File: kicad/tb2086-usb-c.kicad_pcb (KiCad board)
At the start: 2 copper layers, 29.3 x 19.5 mm, 17 parts, among them J1 Conn_01x04, U1 SRV05-4

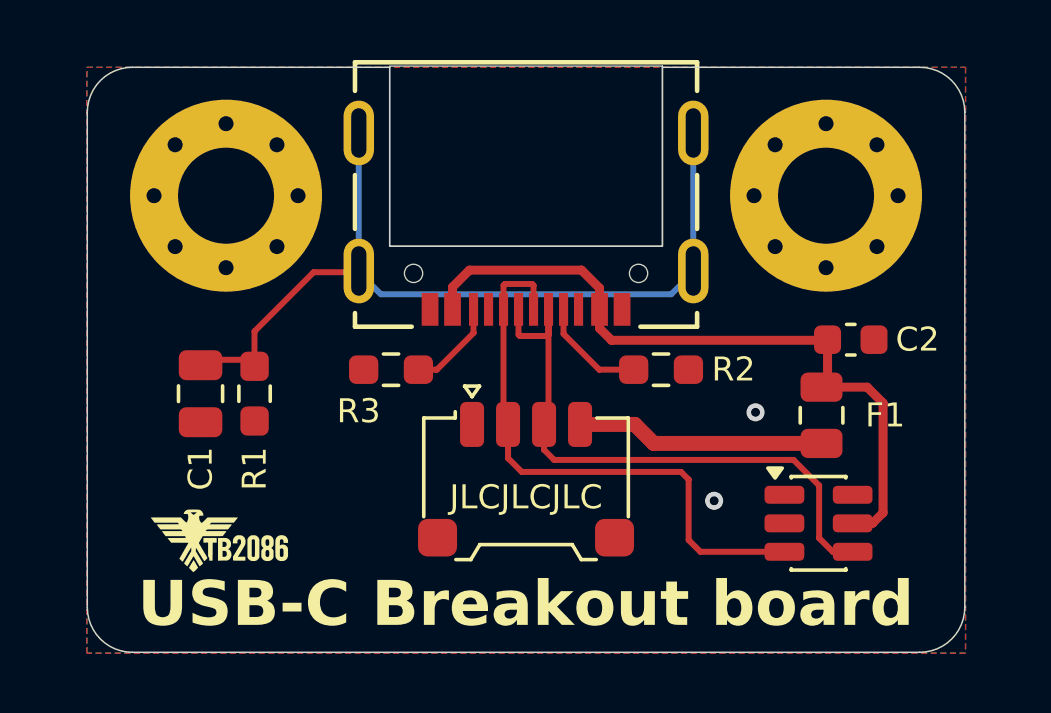
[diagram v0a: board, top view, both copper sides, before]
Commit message: changed ESD protection (#6)
* replaced ESD protection

* updated panelized PCB

* kibot

* fixed zip file name
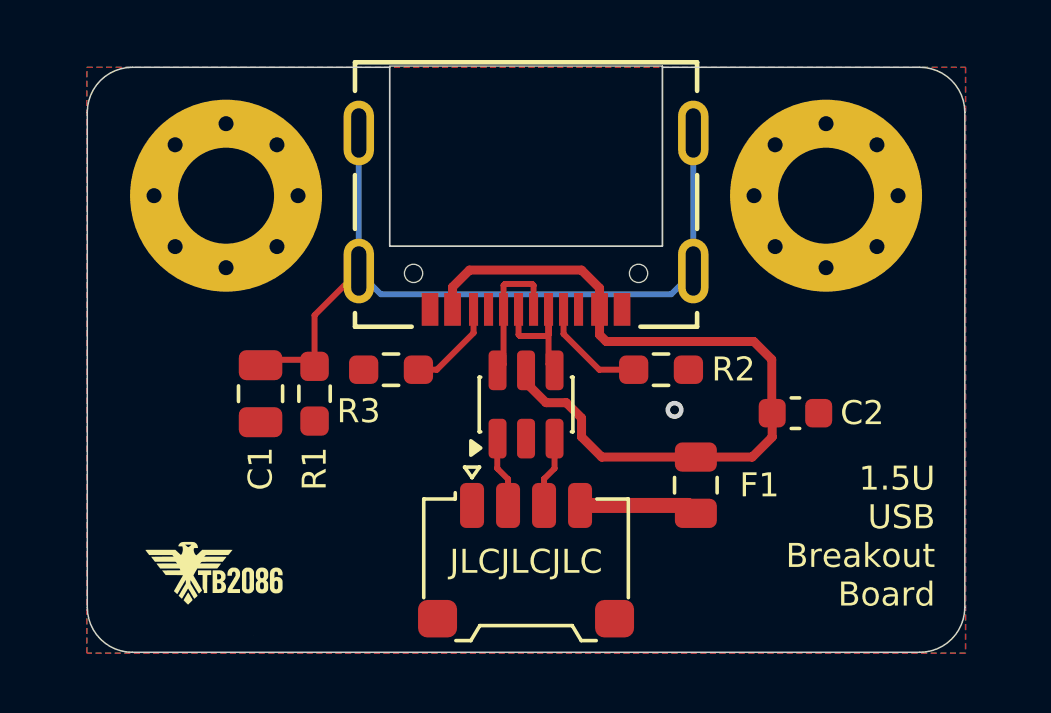
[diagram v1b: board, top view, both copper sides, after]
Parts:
- U1: value SRV05-4 -> USBLC6-2SC6
- moved U1 10.5 mm to (116.5, 69.7), turned to 90 degrees
- moved F1 4.79 mm to (122.2, 72.4)
- moved C2 3.07 mm to (125.5, 70.0)
- moved J1 2.70 mm to (116.5, 75.0)
- moved C1 2.00 mm to (107.7, 69.4)
- moved R1 2.00 mm to (109.5, 69.4)
- moved G*** 1.09 mm to (106.2, 75.3)
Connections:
- U1 pad 1: unconnected-(U1-IO1-Pad1) -> DATA+
- U1 pad 3: DATA+ -> DATA-
- U1 pad 4: DATA- -> USB_DATA-
- U1 pad 6: unconnected-(U1-IO4-Pad6) -> USB_DATA+
- USB1 pad A6: DATA+ -> USB_DATA+
- USB1 pad A7: DATA- -> USB_DATA-
- USB1 pad B6: DATA+ -> USB_DATA+
- USB1 pad B7: DATA- -> USB_DATA-
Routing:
- net DATA-: track 19.9 -> 2.37 mm
- net DATA+: track 19.3 -> 2.38 mm
- net USB_DATA-: track 0.00 -> 4.76 mm
- net USB_DATA+: track 0.00 -> 4.76 mm
- net +5V: track 8.31 -> 3.97 mm
- net VBUS: track 23.5 -> 26.6 mm
- net Net-(USB1-Shield): track 28.0 -> 26.5 mm
- net GND: vias 2 -> 1
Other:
- board text added: "1.5U USB Breakout Board"
- board text added: "2025.11.23"
- board text removed: "2025.11.22"

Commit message: changed footprint (#7)
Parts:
- C2: footprint Capacitor_SMD:C_0603_1608Metric -> Capacitor_SMD:C_0603_1608Metric_Pad1.08x0.95mm_HandSolder
- F1: footprint Fuse:Fuse_0805_2012Metric -> Fuse:Fuse_0805_2012Metric_Pad1.15x1.40mm_HandSolder
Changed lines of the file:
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@@
 		(embedded_fonts no)
 	)
-	(footprint "Fuse:Fuse_0805_2012Metric"
+	(footprint "Fuse:Fuse_0805_2012Metric_Pad1.15x1.40mm_HandSolder"
 		(layer "F.Cu")
 		(at 122.21 72.43 90)
-		(descr "Fuse SMD 0805 (2012 Metric), square (rectangular) end terminal, IPC-7351 nominal, (Body size source: https://docs.google.com/spreadsheets/d/1BsfQQcO9C6DZCsRaXUlFlo91Tg2WpOkGARC1WS5S8t0/edit?usp=sharing), generated with kicad-footprint-generator")
-		(tags "fuse")
+		(descr "Fuse SMD 0805 (2012 Metric), square (rectangular) end terminal, IPC-7351 nominal with elongated pad for handsoldering. (Body size source: https://docs.google.com/spreadsheets/d/1BsfQQcO9C6DZCsRaXUlFlo91Tg2WpOkGARC1WS5S8t0/edit?usp=sharing), generated with kicad-footprint-generator")
+		(tags "fuse handsolder")
 		(property "Reference" "F1"
-			(at 0 2.12 0)
-			(layer "F.SilkS")
-			(effects
-				(font
-					(size 0.8 0.8)
+			(at 0 -1.65 90)
+			(layer "F.SilkS")
+			(effects
+				(font
+					(size 1 1)
 					(thickness 0.15)
 				)
@@
 		(attr smd)
 		(fp_line
-			(start -0.258578 -0.71)
-			(end 0.258578 -0.71)
+			(start -0.261252 -0.71)
+			(end 0.261252 -0.71)
 			(stroke
 				(width 0.12)
@@
 		)
 		(fp_line
-			(start -0.258578 0.71)
-			(end 0.258578 0.71)
+			(start -0.261252 0.71)
+			(end 0.261252 0.71)
 			(stroke
 				(width 0.12)
@@
 		)
 		(fp_line
-			(start 1.68 -0.95)
-			(end 1.68 0.95)
+			(start 1.85 -0.95)
+			(end 1.85 0.95)
 			(stroke
 				(width 0.05)
@@
 		)
 		(fp_line
-			(start -1.68 -0.95)
-			(end 1.68 -0.95)
+			(start -1.85 -0.95)
+			(end 1.85 -0.95)
 			(stroke
 				(width 0.05)
@@
 		)
 		(fp_line
-			(start 1.68 0.95)
-			(end -1.68 0.95)
+			(start 1.85 0.95)
+			(end -1.85 0.95)
 			(stroke
 				(width 0.05)
@@
 		)
 		(fp_line
-			(start -1.68 0.95)
-			(end -1.68 -0.95)
+			(start -1.85 0.95)
+			(end -1.85 -0.95)
 			(stroke
 				(width 0.05)
@@
 		)
 		(pad "1" smd roundrect
-			(at -0.9375 0 90)
-			(size 0.975 1.4)
+			(at -1.025 0 90)
+			(size 1.15 1.4)
 			(layers "F.Cu" "F.Mask" "F.Paste")
-			(roundrect_rratio 0.25)
+			(roundrect_rratio 0.217391)
 			(net 10 "+5V")
 			(pintype "passive")
 		)
 		(pad "2" smd roundrect
-			(at 0.9375 0 90)
-			(size 0.975 1.4)
+			(at 1.025 0 90)
+			(size 1.15 1.4)
 			(layers "F.Cu" "F.Mask" "F.Paste")
-			(roundrect_rratio 0.25)
+			(roundrect_rratio 0.217391)
 			(net 2 "VBUS")
 			(pintype "passive")
@@
 		(embedded_fonts no)
 	)
-	(footprint "Capacitor_SMD:C_0603_1608Metric"
+	(footprint "Capacitor_SMD:C_0603_1608Metric_Pad1.08x0.95mm_HandSolder"
 		(layer "F.Cu")
 		(at 125.53 70.03 180)
-		(descr "Capacitor SMD 0603 (1608 Metric), square (rectangular) end terminal, IPC-7351 nominal, (Body size source: IPC-SM-782 page 76, https://www.pcb-3d.com/wordpress/wp-content/uploads/ipc-sm-782a_amendment_1_and_2.pdf), generated with kicad-footprint-generator")
-		(tags "capacitor")
+		(descr "Capacitor SMD 0603 (1608 Metric), square (rectangular) end terminal, IPC-7351 nominal with elongated pad for handsoldering. (Body size source: IPC-SM-782 page 76, https://www.pcb-3d.com/wordpress/wp-content/uploads/ipc-sm-782a_amendment_1_and_2.pdf), generated with kicad-footprint-generator")
+		(tags "capacitor handsolder")
 		(property "Reference" "C2"
-			(at -2.223842 0.006328 0)
-			(layer "F.SilkS")
-			(effects
-				(font
-					(size 0.8 0.8)
+			(at 0 -1.43 180)
+			(layer "F.SilkS")
+			(effects
+				(font
+					(size 1 1)
 					(thickness 0.15)
 				)
@@
 		)
 		(property "Value" "10u"
-			(at 0 1.43 0)
+			(at 0 1.43 180)
 			(layer "F.Fab")
 			(effects
@@
 		)
 		(property "Datasheet" "~"
-			(at 0 0 0)
+			(at 0 0 180)
 			(layer "F.Fab")
 			(hide yes)
@@
 		)
 		(property "Description" ""
-			(at 0 0 0)
+			(at 0 0 180)
 			(layer "F.Fab")
 			(hide yes)
@@
 		(attr smd)
 		(fp_line
-			(start -0.14058 0.51)
-			(end 0.14058 0.51)
+			(start -0.146267 0.51)
+			(end 0.146267 0.51)
 			(stroke
 				(width 0.12)
@@
 		)
 		(fp_line
-			(start -0.14058 -0.51)
-			(end 0.14058 -0.51)
+			(start -0.146267 -0.51)
+			(end 0.146267 -0.51)
 			(stroke
 				(width 0.12)
@@
 		)
 		(fp_line
-			(start 1.48 0.73)
-			(end -1.48 0.73)
+			(start 1.65 0.73)
+			(end -1.65 0.73)
 			(stroke
 				(width 0.05)
@@
 		)
 		(fp_line
-			(start 1.48 -0.73)
-			(end 1.48 0.73)
+			(start 1.65 -0.73)
+			(end 1.65 0.73)
 			(stroke
 				(width 0.05)
@@
 		)
 		(fp_line
-			(start -1.48 0.73)
-			(end -1.48 -0.73)
+			(start -1.65 0.73)
+			(end -1.65 -0.73)
 			(stroke
 				(width 0.05)
@@
 		)
 		(fp_line
-			(start -1.48 -0.73)
-			(end 1.48 -0.73)
+			(start -1.65 -0.73)
+			(end 1.65 -0.73)
 			(stroke
 				(width 0.05)
@@
 		)
 		(fp_text user "${REFERENCE}"
-			(at 0 0 0)
+			(at 0 0 180)
 			(layer "F.Fab")
 			(effects
@@
 		)
 		(pad "1" smd roundrect
-			(at -0.775 0 180)
-			(size 0.9 0.95)
+			(at -0.8625 0 180)
+			(size 1.075 0.95)
 			(layers "F.Cu" "F.Mask" "F.Paste")
 			(roundrect_rratio 0.25)
 			(net 1 "GND")
 			(pintype "passive")
-			(zone_connect 2)
 		)
 		(pad "2" smd roundrect
-			(at 0.775 0 180)
-			(size 0.9 0.95)
+			(at 0.8625 0 180)
+			(size 1.075 0.95)
 			(layers "F.Cu" "F.Mask" "F.Paste")
 			(roundrect_rratio 0.25)
